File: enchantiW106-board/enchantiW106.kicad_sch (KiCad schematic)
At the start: 70 parts, among them J1 USB_C_Receptacle_USB2.0, SW1 B3U-1000P, SW2 B3U-1000P, U1 USBLC6-2P6, U11 MAX17262REWL+T, U12 BQ25185DLHR, U13 ICM-42670-P, U2 MMC5633NJL, U3 IRIS-W106-00B, U4 NCP167AMX330TBG, U5 CP2102N-Axx-xQFN20, U6 ESP-PSRAM64, U9 NCP167AMX330TBG

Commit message: add initial software files
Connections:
- net CTS: now also U3.A9 (SDIO_D1); no longer U3.N3 (GPIO[53])
- net RTS: now also U3.B8 (SDIO_D0); no longer U3.L4 (RMII_INT)
- net RXD: now also U3.B9 (FC3_RxD); no longer U3.L1 (RMII_MDIO)
- net SCL: now also U3.L2 (RMII_MDC); no longer U3.A10 (FC3_TxD)
- net SDA: now also U3.L1 (RMII_MDIO); no longer U3.B9 (FC3_RxD)
- net TXD: now also U3.A10 (FC3_TxD); no longer U3.L2 (RMII_MDC)
- net UART_CLCK: no longer names the net of U3.M2 (GPIO[21])
- no-connect marks 59 -> 58
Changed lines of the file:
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@@
 	)
 	(no_connect
+		(at 138.43 96.52)
+	)
+	(no_connect
 		(at 262.89 38.1)
 	)
@@
 	)
 	(no_connect
-		(at 187.96 78.74)
-	)
-	(no_connect
 		(at 187.96 68.58)
 	)
@@
 	)
 	(no_connect
-		(at 187.96 76.2)
-	)
-	(no_connect
 		(at 171.45 135.89)
 	)
@@
 	(wire
 		(pts
+			(xy 132.08 109.22) (xy 138.43 109.22)
+		)
+		(stroke
+			(width 0)
+			(type default)
+		)
+	)
+	(wire
+		(pts
 			(xy 379.73 146.05) (xy 391.16 146.05)
 		)
@@
 	(wire
 		(pts
-			(xy 133.35 96.52) (xy 138.43 96.52)
-		)
-		(stroke
-			(width 0)
-			(type default)
-		)
-	)
-	(wire
-		(pts
 			(xy 46.99 96.52) (xy 46.99 92.71)
 		)
@@
 	(wire
 		(pts
+			(xy 187.96 78.74) (xy 195.58 78.74)
+		)
+		(stroke
+			(width 0)
+			(type default)
+		)
+	)
+	(wire
+		(pts
 			(xy 17.78 214.63) (xy 33.02 214.63)
 		)
@@
 	(wire
 		(pts
-			(xy 133.35 109.22) (xy 138.43 109.22)
-		)
-		(stroke
-			(width 0)
-			(type default)
-		)
-	)
-	(wire
-		(pts
 			(xy 118.11 280.67) (xy 127 280.67)
 		)
@@
 	(wire
 		(pts
-			(xy 132.08 88.9) (xy 138.43 88.9)
-		)
-		(stroke
-			(width 0)
-			(type default)
-		)
-	)
-	(wire
-		(pts
 			(xy 297.18 59.69) (xy 312.42 59.69)
 		)
@@
 		)
 	)
-	(wire
-		(pts
-			(xy 133.35 106.68) (xy 138.43 106.68)
-		)
-		(stroke
-			(width 0)
-			(type default)
-		)
-	)
 	(polyline
 		(pts
@@
 	(wire
 		(pts
-			(xy 133.35 121.92) (xy 138.43 121.92)
-		)
-		(stroke
-			(width 0)
-			(type default)
-		)
-	)
-	(wire
-		(pts
 			(xy 391.16 213.36) (xy 391.16 214.63)
 		)
@@
 	(wire
 		(pts
+			(xy 187.96 76.2) (xy 195.58 76.2)
+		)
+		(stroke
+			(width 0)
+			(type default)
+		)
+	)
+	(wire
+		(pts
 			(xy 262.89 63.5) (xy 262.89 68.58)
 		)
@@
 	(wire
 		(pts
+			(xy 132.08 106.68) (xy 138.43 106.68)
+		)
+		(stroke
+			(width 0)
+			(type default)
+		)
+	)
+	(wire
+		(pts
 			(xy 200.66 40.64) (xy 200.66 43.18)
 		)
@@
 		)
 	)
+	(label "SDA"
+		(at 137.16 109.22 180)
+		(fields_autoplaced yes)
+		(effects
+			(font
+				(size 1.27 1.27)
+			)
+			(justify right bottom)
+		)
+	)
 	(label "RD1"
 		(at 58.42 269.24 0)
@@
 		)
 	)
-	(label "SDA"
-		(at 193.04 62.23 180)
-		(fields_autoplaced yes)
-		(effects
-			(font
-				(size 1.27 1.27)
-			)
-			(justify right bottom)
-		)
-	)
-	(label "RXD"
-		(at 137.16 109.22 180)
-		(fields_autoplaced yes)
-		(effects
-			(font
-				(size 1.27 1.27)
-			)
-			(justify right bottom)
-		)
-	)
 	(label "BLUELED"
 		(at 138.43 76.2 180)
@@
 		)
 	)
+	(label "RXD"
+		(at 193.04 62.23 180)
+		(fields_autoplaced yes)
+		(effects
+			(font
+				(size 1.27 1.27)
+			)
+			(justify right bottom)
+		)
+	)
 	(label "LED2"
 		(at 184.15 250.19 180)
@@
 		)
 	)
-	(label "UART_CLCK"
-		(at 138.43 96.52 180)
+	(label "FSR2"
+		(at 137.16 68.58 180)
 		(fields_autoplaced yes)
 		(effects
@@
 	)
 	(label "SCL"
-		(at 193.04 59.69 180)
-		(fields_autoplaced yes)
-		(effects
-			(font
-				(size 1.27 1.27)
-			)
-			(justify right bottom)
-		)
-	)
-	(label "FSR2"
-		(at 137.16 68.58 180)
+		(at 137.16 106.68 180)
 		(fields_autoplaced yes)
 		(effects
@@
 		)
 	)
-	(label "RTS"
-		(at 137.16 121.92 180)
-		(fields_autoplaced yes)
-		(effects
-			(font
-				(size 1.27 1.27)
-			)
-			(justify right bottom)
-		)
-	)
 	(label "SCL2"
 		(at 287.02 82.55 0)
@@
 		)
 	)
-	(label "CTS"
-		(at 137.16 88.9 180)
+	(label "RXD"
+		(at 257.81 165.1 0)
 		(fields_autoplaced yes)
 		(effects
@@
 				(size 1.27 1.27)
 			)
-			(justify right bottom)
+			(justify left bottom)
 		)
 	)
-	(label "RXD"
-		(at 257.81 165.1 0)
+	(label "IO12"
+		(at 193.04 57.15 180)
 		(fields_autoplaced yes)
 		(effects
@@
 				(size 1.27 1.27)
 			)
-			(justify left bottom)
+			(justify right bottom)
 		)
 	)
-	(label "IO12"
-		(at 193.04 57.15 180)
+	(label "RTS"
+		(at 189.23 78.74 0)
 		(fields_autoplaced yes)
 		(effects
@@
 				(size 1.27 1.27)
 			)
-			(justify right bottom)
+			(justify left bottom)
 		)
 	)
@@
 		)
 	)
-	(label "TXD"
-		(at 137.16 106.68 180)
+	(label "STAT2"
+		(at 184.15 252.73 180)
 		(fields_autoplaced yes)
 		(effects
@@
 		)
 	)
-	(label "STAT2"
-		(at 184.15 252.73 180)
+	(label "EN"
+		(at 227.33 165.1 0)
 		(fields_autoplaced yes)
 		(effects
@@
 				(size 1.27 1.27)
 			)
-			(justify right bottom)
+			(justify left bottom)
 		)
 	)
-	(label "EN"
-		(at 227.33 165.1 0)
+	(label "CTS"
+		(at 189.23 76.2 0)
 		(fields_autoplaced yes)
 		(effects
@@
 		)
 	)
+	(label "TXD"
+		(at 193.04 59.69 180)
+		(fields_autoplaced yes)
+		(effects
+			(font
+				(size 1.27 1.27)
+			)
+			(justify right bottom)
+		)
+	)

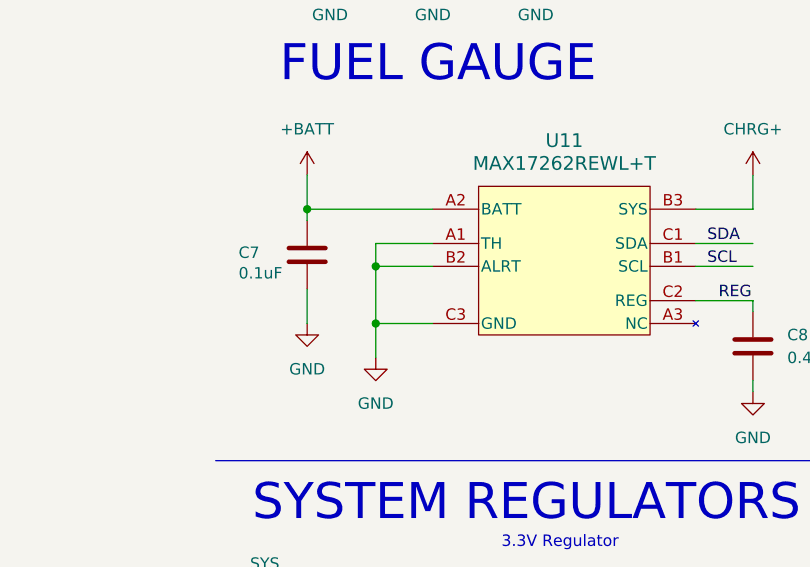
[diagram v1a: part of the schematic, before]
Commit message: add git submodule for libmapper
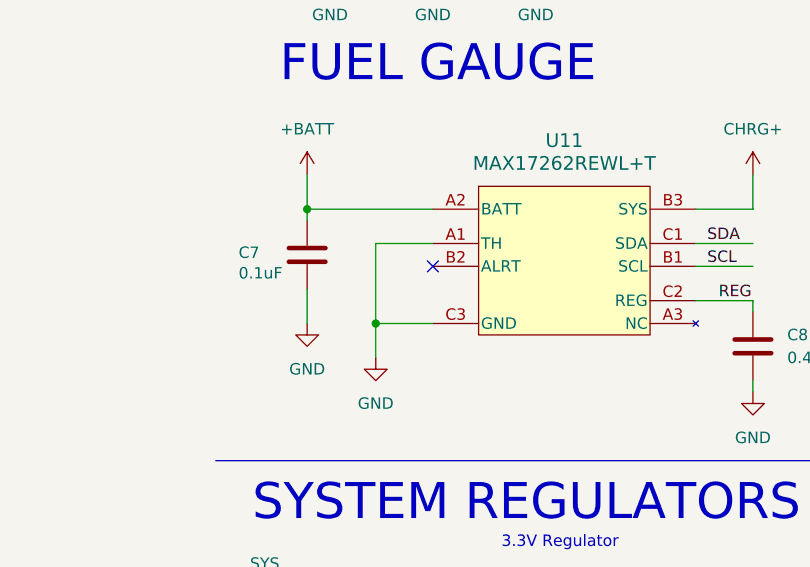
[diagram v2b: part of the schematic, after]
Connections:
- net GND: no longer U11.B2 (ALRT)
- no-connect marks 58 -> 59
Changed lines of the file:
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@@
-	)
-	(junction
-		(at 29.21 129.54)
-		(diameter 0)
-		(color 0 0 0 0)
 	)
 	(junction
@@
 	)
 	(no_connect
+		(at 35.56 129.54)
+	)
+	(no_connect
 		(at 187.96 127)
 	)
@@
 	(wire
 		(pts
-			(xy 29.21 127) (xy 29.21 129.54)
-		)
-		(stroke
-			(width 0)
-			(type default)
-		)
-	)
-	(wire
-		(pts
 			(xy 227.33 180.34) (xy 231.14 180.34)
 		)
@@
 	(wire
 		(pts
-			(xy 29.21 129.54) (xy 35.56 129.54)
-		)
-		(stroke
-			(width 0)
-			(type default)
-		)
-	)
-	(wire
-		(pts
 			(xy 187.96 54.61) (xy 194.31 54.61)
 		)
@@
 	(wire
 		(pts
-			(xy 29.21 129.54) (xy 29.21 135.89)
-		)
-		(stroke
+			(xy 29.21 127) (xy 29.21 135.89)
+		)
+		(stroke

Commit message: added axis labels to pcb silkscreen, fixed incorrect axis of magnetometer and accelerometer
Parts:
- added U7: STM32H562RIVx, Package_DFN_QFN:QFN-68-1EP_8x8mm_P0.4mm_EP6.4x6.4mm, symbol MCU_ST_STM32H5:STM32H562RIVx
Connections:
- new net: U7.18 (VSS), U7.32 (VSS), U7.50 (VSS), U7.67 (VSS), U7.69 (VSS)
